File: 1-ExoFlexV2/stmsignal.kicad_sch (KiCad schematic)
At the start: 4 parts, among them J4 CN8, J5 CN9, J6 CN7, J7 CN10

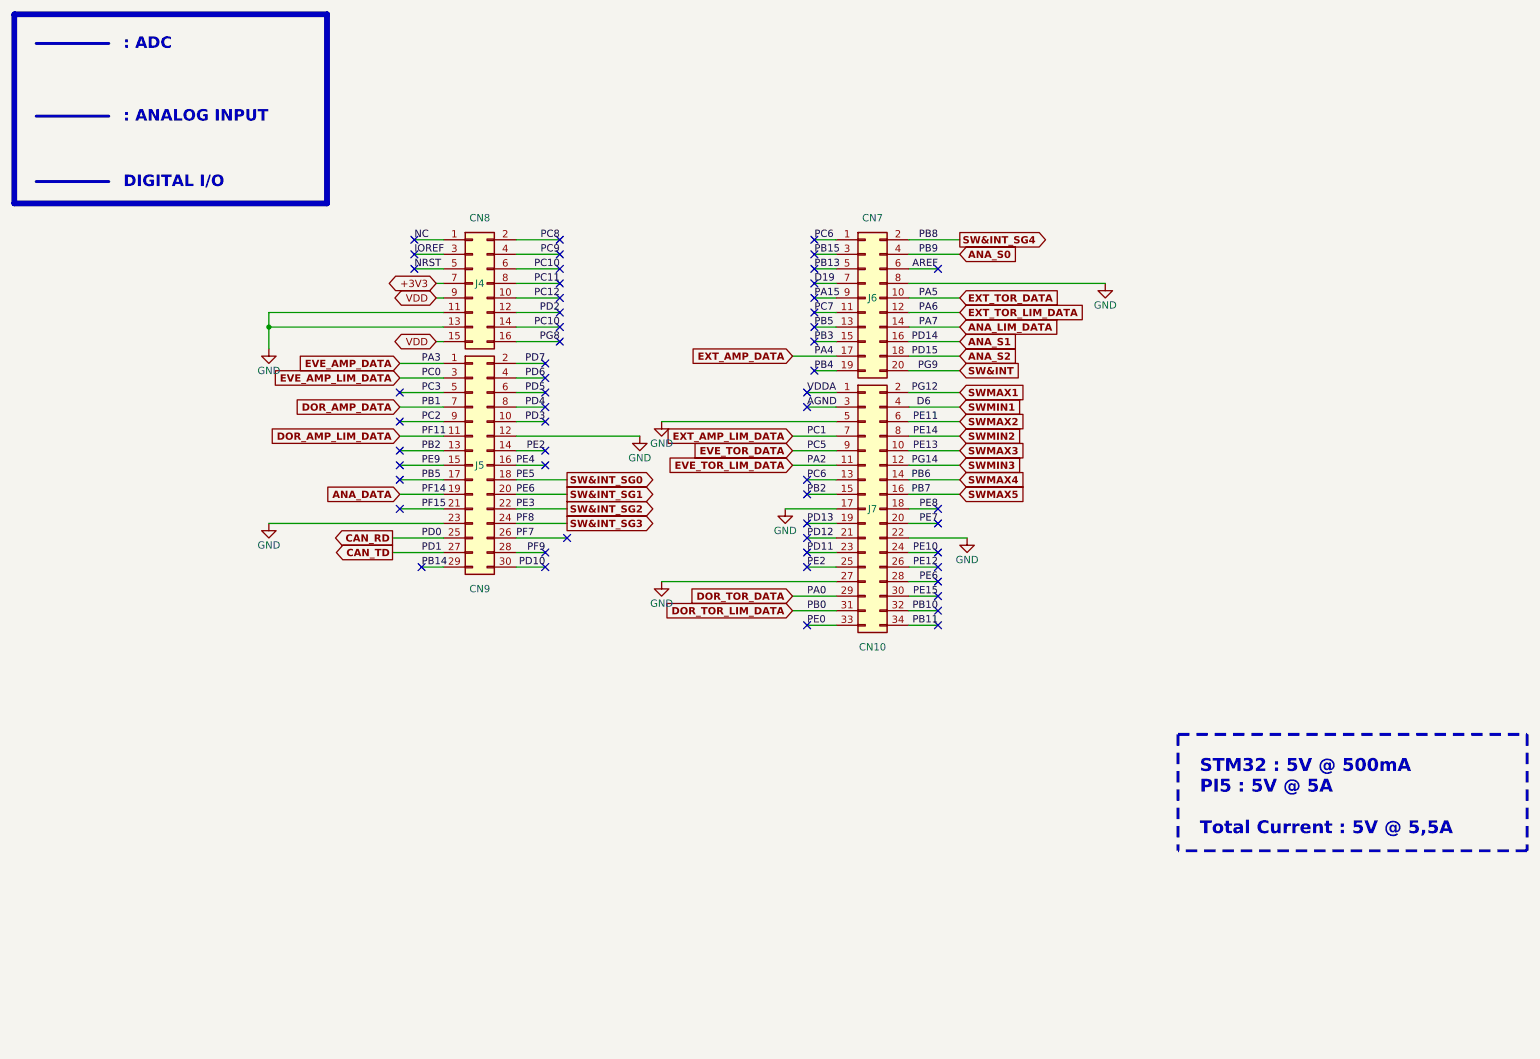
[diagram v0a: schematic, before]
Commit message: Trimmer et jumper
-Changement de symbole de jumper
-Ajout des des trimmer aux endroits nécessaires
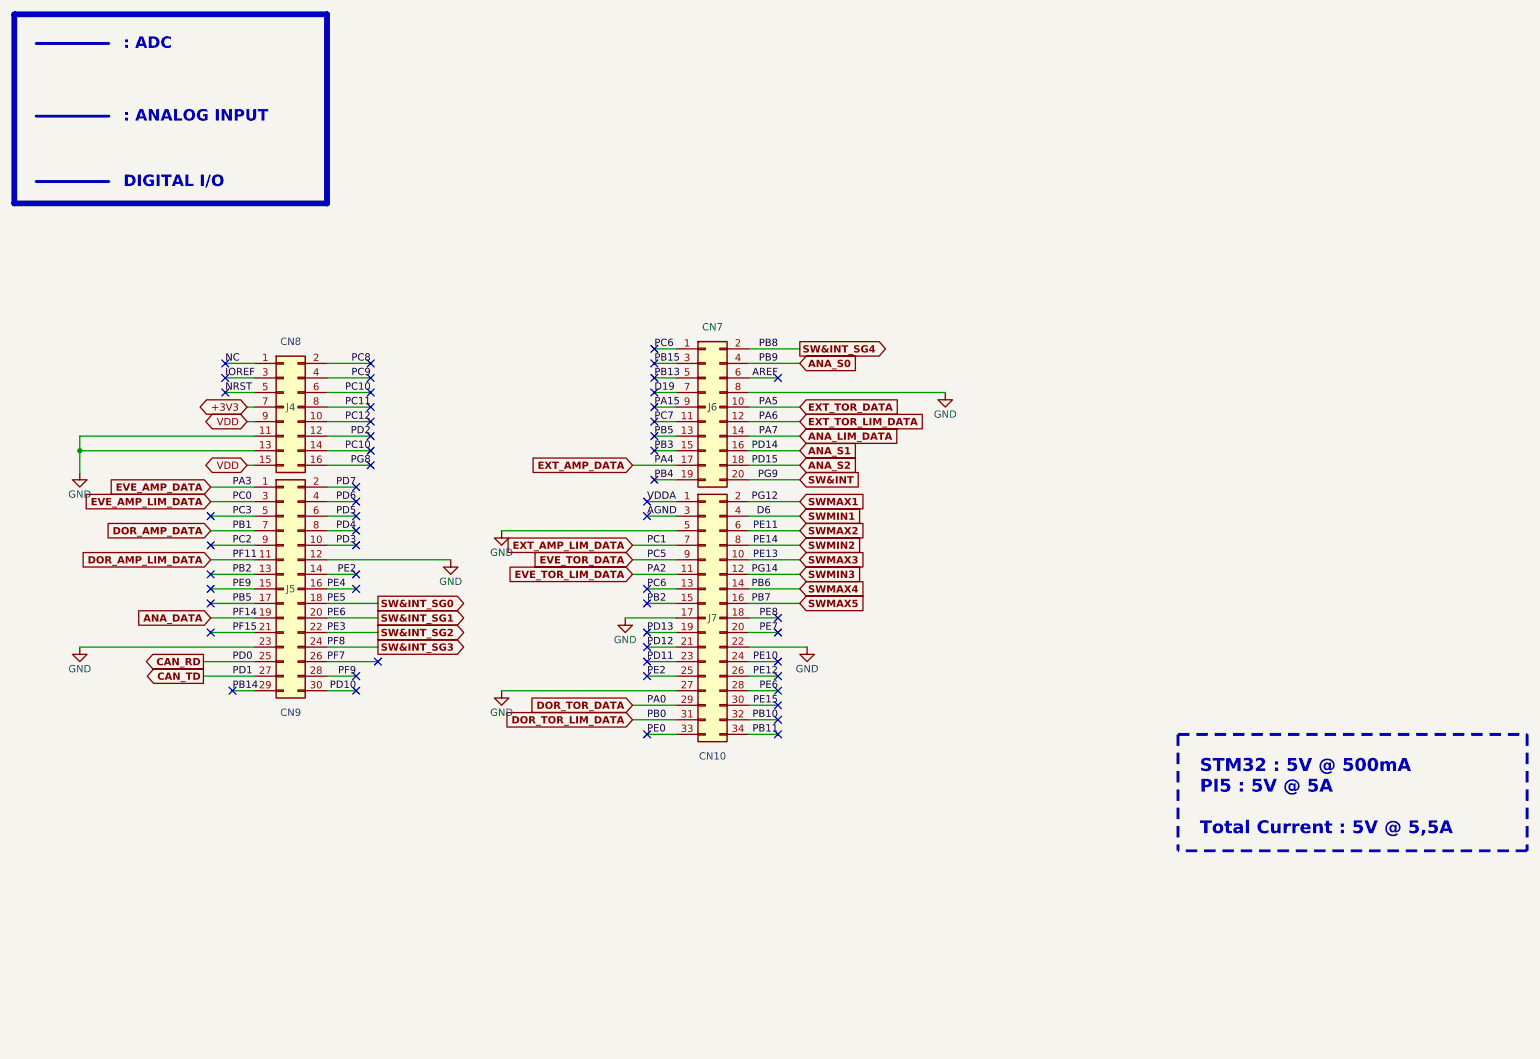
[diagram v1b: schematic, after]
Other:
- moved on the sheet: J4, J5, J6, J7

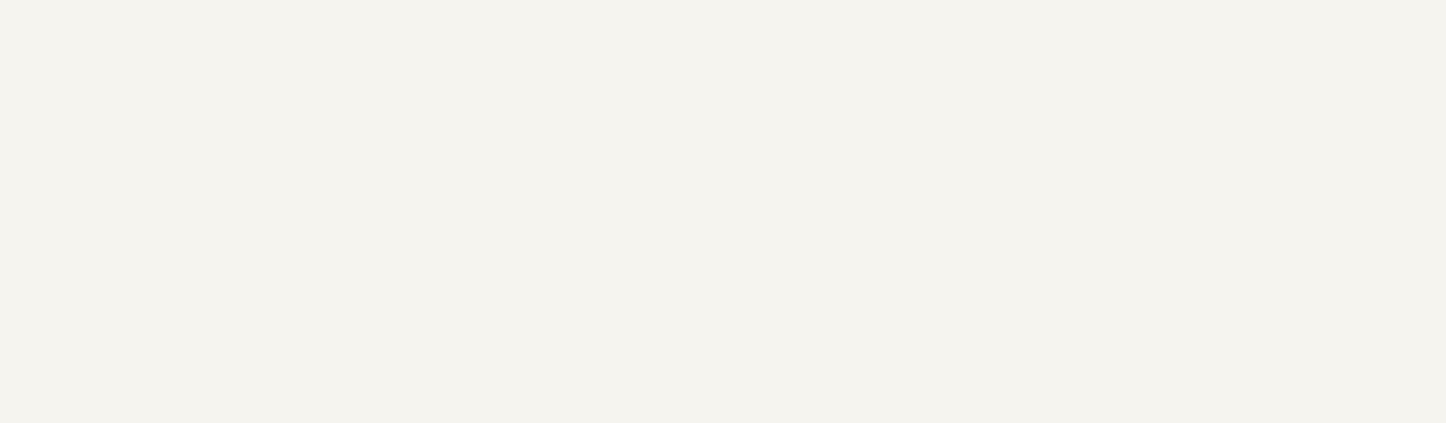
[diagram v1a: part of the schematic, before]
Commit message: Test points et notes
- Ajout de tous les tests point nécessaires
-  Ajoute des sections de notes dans chaque page
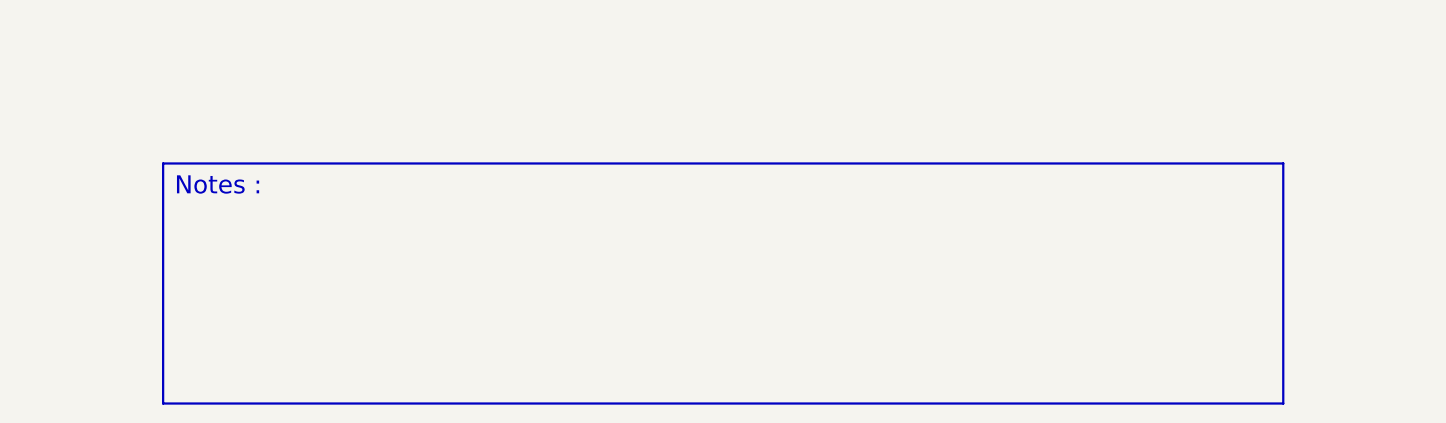
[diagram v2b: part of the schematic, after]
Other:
- note added: "Notes :"
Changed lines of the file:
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@@
     (stroke (width 0) (type default) (color 0 0 0 0))
+  )
+  (polyline (pts (xy 48.26 168.91) (xy 48.26 195.58))
+    (stroke (width 0.25) (type solid) (color 0 0 0 0))
   )
   (wire (pts (xy 53.34 78.74) (xy 58.42 78.74))
@@
   (wire (pts (xy 144.78 73.66) (xy 153.67 73.66))
     (stroke (width 0.5) (type default) (color 255 74 249 1))
+  )
+  (polyline (pts (xy 172.72 168.91) (xy 172.72 195.58))
+    (stroke (width 0.25) (type solid) (color 0 0 0 0))
   )
   (wire (pts (xy 128.27 96.52) (xy 132.08 96.52))
@@
     (stroke (width 0) (type default) (color 0 0 0 0))
   )
+  (polyline (pts (xy 48.26 168.91) (xy 172.72 168.91))
+    (stroke (width 0.25) (type solid) (color 0 0 0 0))
+  )
   (wire (pts (xy 50.8 107.95) (xy 58.42 107.95))
     (stroke (width 0.5) (type default) (color 255 115 33 1))
@@
     (stroke (width 0) (type default) (color 0 0 0 0))
   )
+  (polyline (pts (xy 172.72 195.58) (xy 48.26 195.58))
+    (stroke (width 0.25) (type solid) (color 0 0 0 0))
+  )
   (wire (pts (xy 27.94 88.9) (xy 27.94 91.44))
     (stroke (width 0) (type default) (color 0 0 0 0))
@@
     (stroke (width 0.5) (type default) (color 40 35 255 1))
   )
+  (text "Notes :" (at 49.53 172.72 0)
+    (effects (font (size 2 2)) (justify left bottom))
+  )
   (text "STM32 : 5V @ 500mA\nPI5 : 5V @ 5A\n\nTotal Current : 5V @ 5,5A"

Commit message: Schématisation terminée
- Schéma terminé
- Passage vers le PCB
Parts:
- J10: renamed from J5; footprint Connector_PinSocket_2.54mm:PinSocket_2x15_P2.54mm_Vertical -> FootPrintLib:SAMTEC_SSW-115-01-G-D; DESCRIPTION (none) -> 30 Position Receptacle Connector 0.100" (2.54mm) Through Ho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; MANUFACTURER (none) -> Samtec Inc.; PACKAGE (none) -> 30 POS 0.100" (2.54mm); PART NUMBER (none) -> SSW-115-01-G-D; TYPE (none) -> Through Hole
- J11: renamed from J6; footprint Connector_PinSocket_2.54mm:PinSocket_2x10_P2.54mm_Vertical -> FootPrintLib:SAMTEC_SSW-110-01-G-D; DESCRIPTION (none) -> 20 Position Receptacle Connector 0.100" (2.54mm) Through Ho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; MANUFACTURER (none) -> Samtec Inc.; PACKAGE (none) -> 20 POS 0.100" (2.54mm); PART NUMBER (none) -> SSW-110-01-G-D; TYPE (none) -> Through Hole
- J12: renamed from J7; footprint Connector_PinSocket_2.54mm:PinSocket_2x17_P2.54mm_Vertical -> FootPrintLib:SAMTEC_SSW-117-01-G-D; DESCRIPTION (none) -> 34 Position Receptacle Connector 0.100" (2.54mm) Through Ho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; MANUFACTURER (none) -> Samtec Inc.; PACKAGE (none) -> 34 POS 0.100" (2.54mm); PART NUMBER (none) -> SSW-117-01-G-D; TYPE (none) -> Through Hole
- J9: renamed from J4; footprint Connector_PinSocket_2.54mm:PinSocket_2x08_P2.54mm_Vertical -> FootPrintLib:SAMTEC_SSW-108-01-G-D; DESCRIPTION (none) -> 16 Position Receptacle Connector 0.100" (2.54mm) Through Ho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; MANUFACTURER (none) -> Samtec Inc.; PACKAGE (none) -> 16 POS 0.100" (2.54mm); PART NUMBER (none) -> SSW-108-01-G-D; TYPE (none) -> Through Hole
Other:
- note added: "CN10"
- note added: "CN7"
- note added: "CN8"
- note added: "CN9"
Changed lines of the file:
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@@
   )
   (polyline (pts (xy 219.71 140.97) (xy 219.71 161.29))
-    (stroke (width 0.5) (type dash) (color 255 148 44 1))
+    (stroke (width 0.5) (type dash) (color 37 168 45 1))
   )
   (polyline (pts (xy 280.67 161.29) (xy 219.71 161.29))
-    (stroke (width 0.5) (type dash) (color 255 148 44 1))
+    (stroke (width 0.5) (type dash) (color 37 168 45 1))
   )
   (wire (pts (xy 71.12 102.87) (xy 76.2 102.87))
@@
   )
   (polyline (pts (xy 280.67 140.97) (xy 280.67 161.29))
-    (stroke (width 0.5) (type dash) (color 255 148 44 1))
+    (stroke (width 0.5) (type dash) (color 37 168 45 1))
   )
   (wire (pts (xy 124.46 93.98) (xy 132.08 93.98))
@@
   )
   (polyline (pts (xy 219.71 140.97) (xy 280.67 140.97))
-    (stroke (width 0.5) (type dash) (color 255 148 44 1))
+    (stroke (width 0.5) (type dash) (color 37 168 45 1))
   )
   (wire (pts (xy 71.12 100.33) (xy 76.2 100.33))
@@
   (wire (pts (xy 124.46 107.95) (xy 132.08 107.95))
     (stroke (width 0.5) (type default) (color 40 35 255 1))
+  )
+  (text "CN10" (at 135.89 148.59 0)
+    (effects (font (size 1.27 1.27) (thickness 0.254) bold italic) (justify left bottom))
+  )
+  (text "CN8" (at 62.23 71.12 0)
+    (effects (font (size 1.27 1.27) (thickness 0.254) bold italic) (justify left bottom))
   )
   (text "Notes :" (at 49.53 172.72 0)
@@
     (effects (font (size 2 2) (thickness 0.3) bold) (justify left bottom))
   )
+  (text "CN9" (at 62.23 140.97 0)
+    (effects (font (size 1.27 1.27) (thickness 0.254) bold italic) (justify left bottom))
+  )
   (text "DIGITAL I/O" (at 35.56 45.72 0)
     (effects (font (size 2 2) (thickness 0.3) bold) (justify left bottom))
+  )
+  (text "CN7" (at 135.89 69.85 0)
+    (effects (font (size 1.27 1.27) (thickness 0.254) bold italic) (justify left bottom))
   )
   (text ": ADC" (at 35.56 21.59 0)
@@
   (symbol (lib_id "Connector_Generic:Conn_02x17_Odd_Even") (at 137.16 120.65 0) (unit 1)
     (in_bom yes) (on_board yes)
-    (property "Reference" "J7" (id 0) (at 138.43 120.65 0))
+    (property "Reference" "J12" (id 0) (at 138.43 120.65 0))
     (property "Value" "CN10" (id 1) (at 138.43 144.78 0))
-    (property "Footprint" "Connector_PinSocket_2.54mm:PinSocket_2x17_P2.54mm_Vertical" (id 2) (at 137.16 120.65 0)
+    (property "Footprint" "FootPrintLib:SAMTEC_SSW-117-01-G-D" (id 2) (at 137.16 120.65 0)
       (effects (font (size 1.27 1.27)) hide)
     )
     (property "Datasheet" "~" (id 3) (at 137.16 120.65 0)
+      (effects (font (size 1.27 1.27)) hide)
+    )
+    (property "NOTES" "" (id 4) (at 137.16 120.65 0)
+      (effects (font (size 1.27 1.27)) hide)
+    )
+    (property "TYPE" "Through Hole" (id 5) (at 137.16 120.65 0)
+      (effects (font (size 1.27 1.27)) hide)
+    )
+    (property "DESCRIPTION" "34 Position Receptacle Connector 0.100\" (2.54mm) Through Hole Gold" (id 6) (at 137.16 120.65 0)
+      (effects (font (size 1.27 1.27)) hide)
+    )
+    (property "MANUFACTURER" "Samtec Inc." (id 7) (at 137.16 120.65 0)
+      (effects (font (size 1.27 1.27)) hide)
+    )
+    (property "PACKAGE" "34 POS 0.100\" (2.54mm)" (id 8) (at 137.16 120.65 0)
+      (effects (font (size 1.27 1.27)) hide)
+    )
+    (property "PART NUMBER" "SSW-117-01-G-D" (id 9) (at 137.16 120.65 0)
       (effects (font (size 1.27 1.27)) hide)
     )
@@
   (symbol (lib_id "Connector_Generic:Conn_02x15_Odd_Even") (at 63.5 115.57 0) (unit 1)
     (in_bom yes) (on_board yes)
-    (property "Reference" "J5" (id 0) (at 64.77 115.57 0))
+    (property "Reference" "J10" (id 0) (at 64.77 115.57 0))
     (property "Value" "CN9" (id 1) (at 64.77 137.16 0))
-    (property "Footprint" "Connector_PinSocket_2.54mm:PinSocket_2x15_P2.54mm_Vertical" (id 2) (at 63.5 115.57 0)
+    (property "Footprint" "FootPrintLib:SAMTEC_SSW-115-01-G-D" (id 2) (at 63.5 115.57 0)
       (effects (font (size 1.27 1.27)) hide)
     )
     (property "Datasheet" "~" (id 3) (at 63.5 115.57 0)
+      (effects (font (size 1.27 1.27)) hide)
+    )
+    (property "NOTES" "" (id 4) (at 63.5 115.57 0)
+      (effects (font (size 1.27 1.27)) hide)
+    )
+    (property "TYPE" "Through Hole" (id 5) (at 63.5 115.57 0)
+      (effects (font (size 1.27 1.27)) hide)
+    )
+    (property "DESCRIPTION" "30 Position Receptacle Connector 0.100\" (2.54mm) Through Hole Gold" (id 6) (at 63.5 115.57 0)
+      (effects (font (size 1.27 1.27)) hide)
+    )
+    (property "MANUFACTURER" "Samtec Inc." (id 7) (at 63.5 115.57 0)
+      (effects (font (size 1.27 1.27)) hide)
+    )
+    (property "PACKAGE" "30 POS 0.100\" (2.54mm)" (id 8) (at 63.5 115.57 0)
+      (effects (font (size 1.27 1.27)) hide)
+    )
+    (property "PART NUMBER" "SSW-115-01-G-D" (id 9) (at 63.5 115.57 0)
       (effects (font (size 1.27 1.27)) hide)
     )
@@
   (symbol (lib_id "Connector_Generic:Conn_02x08_Odd_Even") (at 63.5 83.82 0) (unit 1)
     (in_bom yes) (on_board yes)
-    (property "Reference" "J4" (id 0) (at 64.77 83.82 0))
+    (property "Reference" "J9" (id 0) (at 64.77 83.82 0))
     (property "Value" "CN8" (id 1) (at 64.77 72.39 0))
-    (property "Footprint" "Connector_PinSocket_2.54mm:PinSocket_2x08_P2.54mm_Vertical" (id 2) (at 63.5 83.82 0)
+    (property "Footprint" "FootPrintLib:SAMTEC_SSW-108-01-G-D" (id 2) (at 63.5 83.82 0)
       (effects (font (size 1.27 1.27)) hide)
     )
     (property "Datasheet" "~" (id 3) (at 63.5 83.82 0)
+      (effects (font (size 1.27 1.27)) hide)
+    )
+    (property "DESCRIPTION" "16 Position Receptacle Connector 0.100\" (2.54mm) Through Hole Gold" (id 4) (at 63.5 83.82 0)
+      (effects (font (size 1.27 1.27)) hide)
+    )
+    (property "MANUFACTURER" "Samtec Inc." (id 5) (at 63.5 83.82 0)
+      (effects (font (size 1.27 1.27)) hide)
+    )
+    (property "PACKAGE" "16 POS 0.100\" (2.54mm)" (id 6) (at 63.5 83.82 0)
+      (effects (font (size 1.27 1.27)) hide)
+    )
+    (property "PART NUMBER" "SSW-108-01-G-D" (id 7) (at 63.5 83.82 0)
+      (effects (font (size 1.27 1.27)) hide)
+    )
+    (property "TYPE" "Through Hole" (id 8) (at 63.5 83.82 0)
       (effects (font (size 1.27 1.27)) hide)
     )
@@
   (symbol (lib_id "power:GND") (at 101.6 105.41 0) (unit 1)
     (in_bom yes) (on_board yes)
-    (property "Reference" "#PWR031" (id 0) (at 101.6 111.76 0)
+    (property "Reference" "#PWR040" (id 0) (at 101.6 111.76 0)
       (effects (font (size 1.27 1.27)) hide)
     )
@@
   (symbol (lib_id "power:GND") (at 27.94 95.25 0) (unit 1)
     (in_bom yes) (on_board yes)
-    (property "Reference" "#PWR028" (id 0) (at 27.94 101.6 0)
+    (property "Reference" "#PWR037" (id 0) (at 27.94 101.6 0)
       (effects (font (size 1.27 1.27)) hide)
     )
@@
   (symbol (lib_id "power:GND") (at 92.71 110.49 0) (unit 1)
     (in_bom yes) (on_board yes)
-    (property "Reference" "#PWR030" (id 0) (at 92.71 116.84 0)
+    (property "Reference" "#PWR039" (id 0) (at 92.71 116.84 0)
       (effects (font (size 1.27 1.27)) hide)
     )
@@
   (symbol (lib_id "power:GND") (at 123.19 120.65 0) (unit 1)
     (in_bom yes) (on_board yes)
-    (property "Reference" "#PWR033" (id 0) (at 123.19 127 0)
+    (property "Reference" "#PWR042" (id 0) (at 123.19 127 0)
       (effects (font (size 1.27 1.27)) hide)
     )
@@
   (symbol (lib_id "power:GND") (at 154.94 125.73 0) (unit 1)
     (in_bom yes) (on_board yes)
-    (property "Reference" "#PWR034" (id 0) (at 154.94 132.08 0)
+    (property "Reference" "#PWR043" (id 0) (at 154.94 132.08 0)
       (effects (font (size 1.27 1.27)) hide)
     )
@@
   (symbol (lib_id "power:GND") (at 101.6 133.35 0) (unit 1)
     (in_bom yes) (on_board yes)
-    (property "Reference" "#PWR032" (id 0) (at 101.6 139.7 0)
+    (property "Reference" "#PWR041" (id 0) (at 101.6 139.7 0)
       (effects (font (size 1.27 1.27)) hide)
     )
@@
   (symbol (lib_id "power:GND") (at 179.07 81.28 0) (unit 1)
     (in_bom yes) (on_board yes)
-    (property "Reference" "#PWR035" (id 0) (at 179.07 87.63 0)
+    (property "Reference" "#PWR044" (id 0) (at 179.07 87.63 0)
       (effects (font (size 1.27 1.27)) hide)
     )
@@
   (symbol (lib_id "Connector_Generic:Conn_02x10_Odd_Even") (at 137.16 83.82 0) (unit 1)
     (in_bom yes) (on_board yes)
-    (property "Reference" "J6" (id 0) (at 138.43 83.82 0))
+    (property "Reference" "J11" (id 0) (at 138.43 83.82 0))
     (property "Value" "CN7" (id 1) (at 138.43 69.85 0))
-    (property "Footprint" "Connector_PinSocket_2.54mm:PinSocket_2x10_P2.54mm_Vertical" (id 2) (at 137.16 83.82 0)
+    (property "Footprint" "FootPrintLib:SAMTEC_SSW-110-01-G-D" (id 2) (at 137.16 83.82 0)
       (effects (font (size 1.27 1.27)) hide)
     )
     (property "Datasheet" "~" (id 3) (at 137.16 83.82 0)
+      (effects (font (size 1.27 1.27)) hide)
+    )
+    (property "DESCRIPTION" "20 Position Receptacle Connector 0.100\" (2.54mm) Through Hole Gold" (id 4) (at 137.16 83.82 0)
+      (effects (font (size 1.27 1.27)) hide)
+    )
+    (property "MANUFACTURER" "Samtec Inc." (id 5) (at 137.16 83.82 0)
+      (effects (font (size 1.27 1.27)) hide)
+    )
+    (property "PACKAGE" "20 POS 0.100\" (2.54mm)" (id 6) (at 137.16 83.82 0)
+      (effects (font (size 1.27 1.27)) hide)
+    )
+    (property "PART NUMBER" "SSW-110-01-G-D" (id 7) (at 137.16 83.82 0)
+      (effects (font (size 1.27 1.27)) hide)
+    )
+    (property "TYPE" "Through Hole" (id 8) (at 137.16 83.82 0)
       (effects (font (size 1.27 1.27)) hide)
     )
@@
   (symbol (lib_id "power:GND") (at 27.94 125.73 0) (unit 1)
     (in_bom yes) (on_board yes)
-    (property "Reference" "#PWR029" (id 0) (at 27.94 132.08 0)
-      (effects (font (size 1.27 1.27)) hide)
-    )
+    (property "Reference" "#PWR038" (id 0) (at 27.94 132.08 0)
+      (effects (font (size 1.27 1.27)) hide)
+    )
